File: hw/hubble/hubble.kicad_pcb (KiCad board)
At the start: 4 copper layers, 41 parts, among them J1 UART, J2 Barrel_Jack_Switch, J3 AVR-ISP-6, J4 JST_EH_S5B-EH, J5 JST_EH_S5B-EH, J6 OLED_Display, SW1 PEC12R-2120F-S0012, SW2 PEC12R-2120F-S0012, SW3 SW_RESET, U1 ATmega88PB-A, U2 MIC5365-3.3YC5, U3 DRTR5V0U4S-7

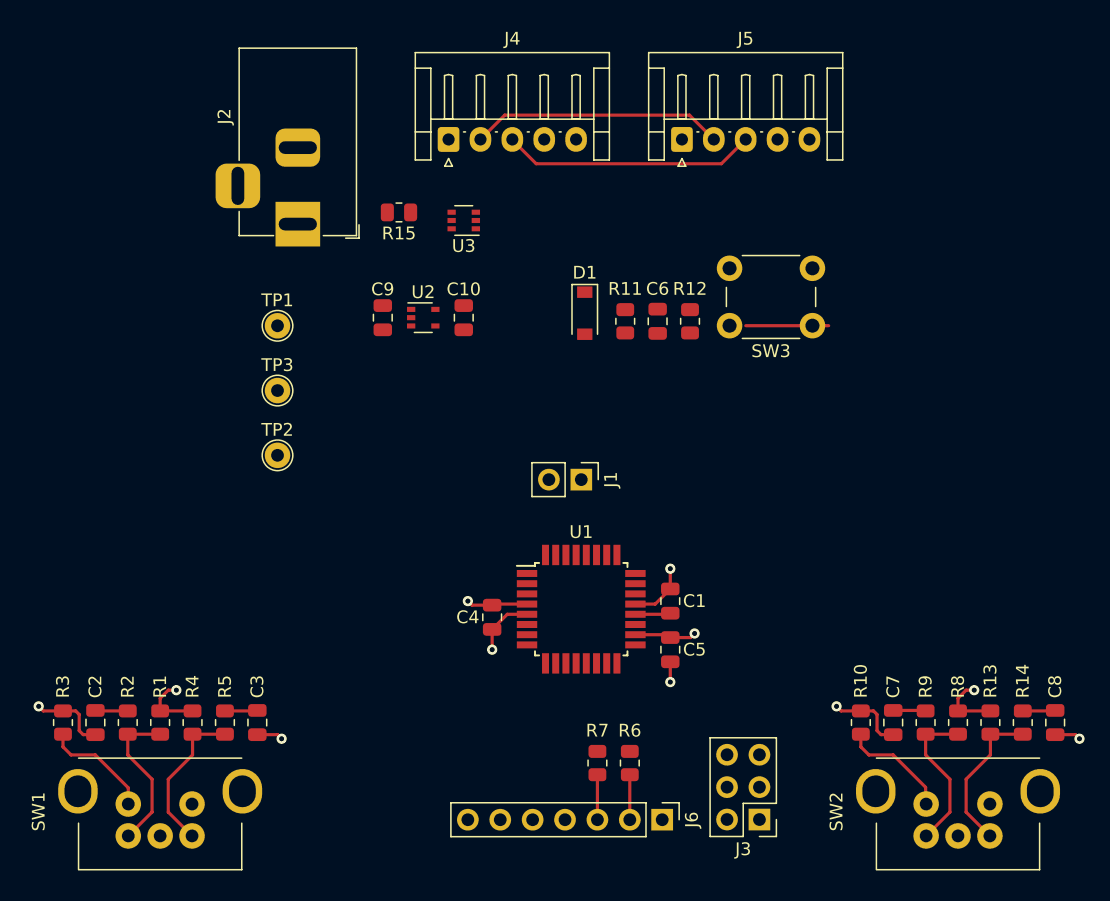
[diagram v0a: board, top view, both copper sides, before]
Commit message: Add reverse polarity protection, more layout
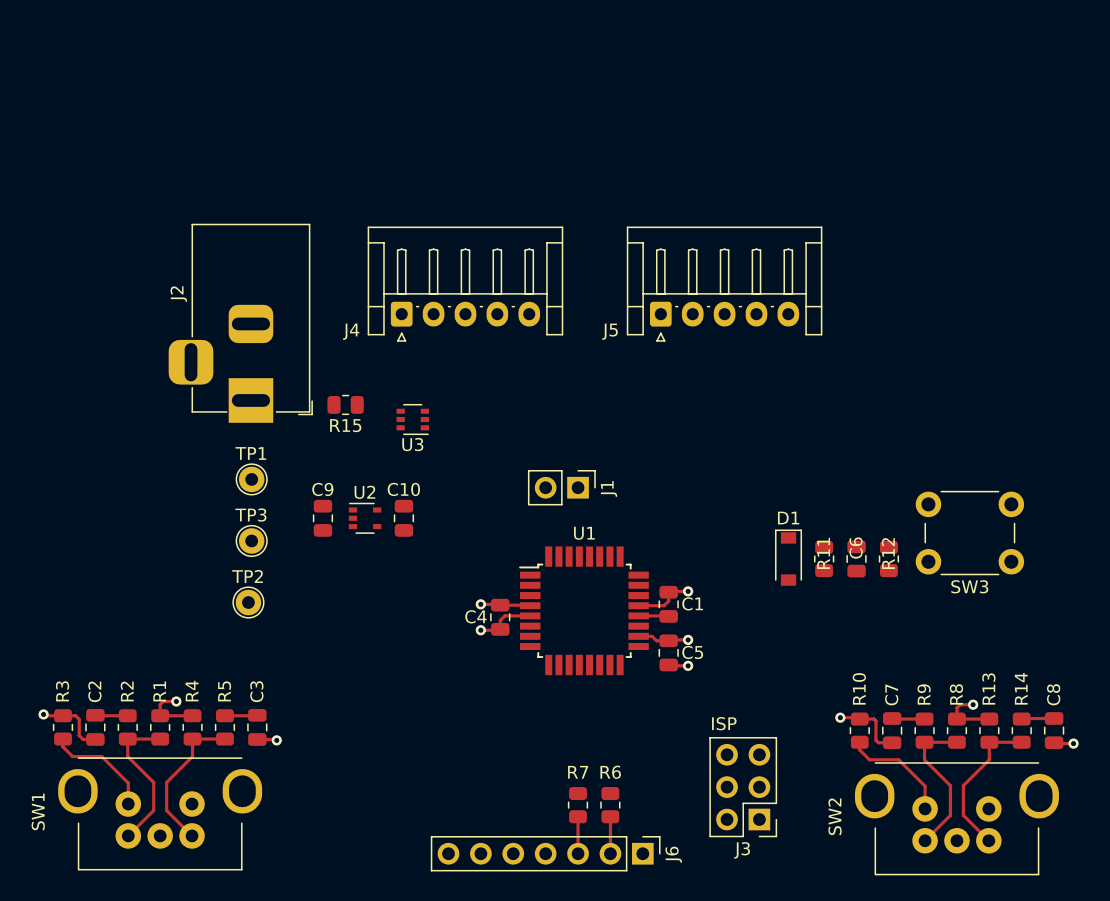
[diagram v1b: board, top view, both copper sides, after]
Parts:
- moved D1 25.0 mm to (150.9, 114.8)
- moved C6 24.3 mm to (156.2, 114.8)
- moved R11 24.3 mm to (153.7, 114.8)
- moved R12 24.3 mm to (158.8, 114.8)
- moved SW3 24.2 mm to (168.3, 115.0)
- moved C10 16.4 mm to (120.7, 111.6)
- moved C9 16.4 mm to (114.4, 111.6)
- moved U2 16.4 mm to (117.7, 111.6)
- moved U3 16.1 mm to (121.4, 103.9)
- moved R15 15.7 mm to (116.1, 102.7)
- moved J2 14.3 mm to (108.7, 102.4)
- moved J4 14.2 mm to (120.5, 95.6)
- moved J5 13.8 mm to (140.9, 95.6)
- moved TP1 12.2 mm to (108.8, 108.6)
- moved TP3 12.0 mm to (108.8, 113.4)
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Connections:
- U1 pad 1: /ENC1_B -> /ENC1_A
- U1 pad 10: /ENC2_B -> unconnected-(U1-Pad10)
- U1 pad 11: /ENC2_SW -> unconnected-(U1-Pad11)
- U1 pad 2: /ENC1_SW -> /ENC1_B
- U1 pad 23: unconnected-(U1-Pad23) -> /ENC2_SW
- U1 pad 24: unconnected-(U1-Pad24) -> /ENC2_A
- U1 pad 25: unconnected-(U1-Pad25) -> /ENC2_B
- U1 pad 32: /ENC1_A -> /ENC1_SW
- U1 pad 9: /ENC2_A -> unconnected-(U1-Pad9)
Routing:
- net /RING_SCL: track 19.9 -> 0.00 mm
- net /RING_SDA: track 19.9 -> 0.00 mm
- net Net-(R12-Pad2): track 6.50 -> 0.00 mm
- net +3.3V: track 19.8 -> 17.5 mm
- net GND: track 27.5 -> 25.5 mm
- net /DISP_SDA: track 3.53 -> 2.90 mm
- net /DISP_SCL: track 3.53 -> 2.90 mm
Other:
- board text added: "ISP"
